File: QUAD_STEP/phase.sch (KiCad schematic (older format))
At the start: 12 parts, among them Q1 BUK9K45-100E,115, Q2 BUK9K45-100E,115

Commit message: beginning layout
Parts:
- Q1, Q2: footprint CUSTOM_FP:TRANS_BUK7K12-60EX -> CUSTOM:TRANS_BUK7K12-60EX; DPN (none) -> 1727-7272-1-ND; MPN (none) -> BUK9K45-100E,115
- R91, R92, R93, R94, R96, R97: footprint (none) -> Resistor_SMD:R_0603_1608Metric_Pad1.05x0.95mm_HandSolder
- R95: footprint (none) -> CUSTOM:WSH2818R0500FEA
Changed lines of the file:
@@
 $Descr A4 11693 8268
 encoding utf-8
-Sheet 3 13
+Sheet 4 13
 Title ""
 Date ""
@@
 AR Path="/5E50B60F/5E4B900F/5E30367B" Ref="Q13"  Part="1"
 AR Path="/5E50B60F/5E4B9032/5E30367B" Ref="Q15"  Part="1"
-F 0 "Q1" H 5400 3000 50  0000 L CNN
+F 0 "Q15" H 5400 3000 50  0000 L CNN
 F 1 "BUK9K45-100E,115" H 5487 2905 50  0001 L CNN
-F 2 "CUSTOM_FP:TRANS_BUK7K12-60EX" H 5400 2875 50  0001 L CIN
+F 2 "CUSTOM:TRANS_BUK7K12-60EX" H 5400 2875 50  0001 L CIN
 F 3 "https://assets.nexperia.com/documents/data-sheet/BUK9K45-100E.pdf" H 5200 2950 50  0001 L CNN
+F 4 "1727-7272-1-ND" H 5200 2950 50  0001 C CNN "DPN"
+F 5 "BUK9K45-100E,115" H 5200 2950 50  0001 C CNN "MPN"
 	1    5200 2950
 	1    0    0    -1
@@
 AR Path="/5E50B60F/5E4B900F/5E303682" Ref="Q14"  Part="1"
 AR Path="/5E50B60F/5E4B9032/5E303682" Ref="Q16"  Part="1"
-F 0 "Q2" H 6300 3000 50  0000 L CNN
+F 0 "Q16" H 6300 3000 50  0000 L CNN
 F 1 "BUK9K45-100E,115" H 6388 2905 50  0001 L CNN
-F 2 "CUSTOM_FP:TRANS_BUK7K12-60EX" H 6300 2875 50  0001 L CIN
+F 2 "CUSTOM:TRANS_BUK7K12-60EX" H 6300 2875 50  0001 L CIN
 F 3 "https://assets.nexperia.com/documents/data-sheet/BUK9K45-100E.pdf" H 6100 2950 50  0001 L CNN
+F 4 "1727-7272-1-ND" H 6100 2950 50  0001 C CNN "DPN"
+F 5 "BUK9K45-100E,115" H 6100 2950 50  0001 C CNN "MPN"
 	1    6100 2950
 	-1   0    0    -1
@@
 AR Path="/5E50B60F/5E4B900F/5E303689" Ref="Q13"  Part="2"
 AR Path="/5E50B60F/5E4B9032/5E303689" Ref="Q15"  Part="2"
-F 0 "Q1" H 5400 4250 50  0000 L CNN
+F 0 "Q15" H 5400 4250 50  0000 L CNN
 F 1 "BUK9K45-100E,115" H 5487 4155 50  0001 L CNN
-F 2 "CUSTOM_FP:TRANS_BUK7K12-60EX" H 5400 4125 50  0001 L CIN
+F 2 "CUSTOM:TRANS_BUK7K12-60EX" H 5400 4125 50  0001 L CIN
 F 3 "https://assets.nexperia.com/documents/data-sheet/BUK9K45-100E.pdf" H 5200 4200 50  0001 L CNN
+F 4 "1727-7272-1-ND" H 5200 4200 50  0001 C CNN "DPN"
+F 5 "BUK9K45-100E,115" H 5200 4200 50  0001 C CNN "MPN"
 	2    5200 4200
 	1    0    0    -1
@@
 AR Path="/5E50B60F/5E4B900F/5E303690" Ref="Q14"  Part="2"
 AR Path="/5E50B60F/5E4B9032/5E303690" Ref="Q16"  Part="2"
-F 0 "Q2" H 6300 4250 50  0000 L CNN
+F 0 "Q16" H 6300 4250 50  0000 L CNN
 F 1 "BUK9K45-100E,115" H 6388 4155 50  0001 L CNN
-F 2 "CUSTOM_FP:TRANS_BUK7K12-60EX" H 6300 4125 50  0001 L CIN
+F 2 "CUSTOM:TRANS_BUK7K12-60EX" H 6300 4125 50  0001 L CIN
 F 3 "https://assets.nexperia.com/documents/data-sheet/BUK9K45-100E.pdf" H 6100 4200 50  0001 L CNN
+F 4 "1727-7272-1-ND" H 6100 4200 50  0001 C CNN "DPN"
+F 5 "BUK9K45-100E,115" H 6100 4200 50  0001 C CNN "MPN"
 	2    6100 4200
 	-1   0    0    -1
@@
 AR Path="/5E50B60F/5E4B900F/5E30369F" Ref="R152"  Part="1"
 AR Path="/5E50B60F/5E4B9032/5E30369F" Ref="R159"  Part="1"
-F 0 "R95" V 5550 4850 50  0000 C CNN
+F 0 "R159" V 5550 4850 50  0000 C CNN
 F 1 "0R022" V 5750 4850 50  0000 C CNN
-F 2 "" V 5580 4850 50  0001 C CNN
+F 2 "CUSTOM:WSH2818R0500FEA" V 5580 4850 50  0001 C CNN
 F 3 "~" H 5650 4850 50  0001 C CNN
 F 4 "WSHM2818R0220FEA" H 5650 4850 50  0001 C CNN "MPN"
@@
 AR Path="/5E50B60F/5E4B900F/5E3036A9" Ref="R149"  Part="1"
 AR Path="/5E50B60F/5E4B9032/5E3036A9" Ref="R156"  Part="1"
-F 0 "R92" V 4700 4200 50  0000 C CNN
+F 0 "R156" V 4700 4200 50  0000 C CNN
 F 1 "22R" V 4900 4200 50  0000 C CNN
-F 2 "" V 4730 4200 50  0001 C CNN
+F 2 "Resistor_SMD:R_0603_1608Metric_Pad1.05x0.95mm_HandSolder" V 4730 4200 50  0001 C CNN
 F 3 "~" H 4800 4200 50  0001 C CNN
 F 4 "ERJ-3EKF22R0V" H 4800 4200 50  0001 C CNN "MPN"
@@
 AR Path="/5E50B60F/5E4B900F/5E3036B3" Ref="R154"  Part="1"
 AR Path="/5E50B60F/5E4B9032/5E3036B3" Ref="R161"  Part="1"
-F 0 "R97" V 6400 4200 50  0000 C CNN
+F 0 "R161" V 6400 4200 50  0000 C CNN
 F 1 "22R" V 6600 4200 50  0000 C CNN
-F 2 "" V 6430 4200 50  0001 C CNN
+F 2 "Resistor_SMD:R_0603_1608Metric_Pad1.05x0.95mm_HandSolder" V 6430 4200 50  0001 C CNN
 F 3 "~" H 6500 4200 50  0001 C CNN
 F 4 "ERJ-3EKF22R0V" H 6500 4200 50  0001 C CNN "MPN"
@@
 AR Path="/5E50B60F/5E4B900F/5E3036BD" Ref="R153"  Part="1"
 AR Path="/5E50B60F/5E4B9032/5E3036BD" Ref="R160"  Part="1"
-F 0 "R96" V 6400 2950 50  0000 C CNN
+F 0 "R160" V 6400 2950 50  0000 C CNN
 F 1 "22R" V 6600 2950 50  0000 C CNN
-F 2 "" V 6430 2950 50  0001 C CNN
+F 2 "Resistor_SMD:R_0603_1608Metric_Pad1.05x0.95mm_HandSolder" V 6430 2950 50  0001 C CNN
 F 3 "~" H 6500 2950 50  0001 C CNN
 F 4 "ERJ-3EKF22R0V" H 6500 2950 50  0001 C CNN "MPN"
@@
 AR Path="/5E50B60F/5E4B900F/5E3036C7" Ref="R148"  Part="1"
 AR Path="/5E50B60F/5E4B9032/5E3036C7" Ref="R155"  Part="1"
-F 0 "R91" V 4700 2950 50  0000 C CNN
+F 0 "R155" V 4700 2950 50  0000 C CNN
 F 1 "22R" V 4900 2950 50  0000 C CNN
-F 2 "" V 4730 2950 50  0001 C CNN
+F 2 "Resistor_SMD:R_0603_1608Metric_Pad1.05x0.95mm_HandSolder" V 4730 2950 50  0001 C CNN
 F 3 "~" H 4800 2950 50  0001 C CNN
 F 4 "ERJ-3EKF22R0V" H 4800 2950 50  0001 C CNN "MPN"
@@
 AR Path="/5E50B60F/5E4B900F/5E3036D1" Ref="R150"  Part="1"
 AR Path="/5E50B60F/5E4B9032/5E3036D1" Ref="R157"  Part="1"
-F 0 "R93" V 5000 4650 50  0000 C CNN
+F 0 "R157" V 5000 4650 50  0000 C CNN
 F 1 "47R" V 5200 4650 50  0000 C CNN
-F 2 "" V 5030 4650 50  0001 C CNN
+F 2 "Resistor_SMD:R_0603_1608Metric_Pad1.05x0.95mm_HandSolder" V 5030 4650 50  0001 C CNN
 F 3 "~" H 5100 4650 50  0001 C CNN
 F 4 "CRGCQ0603F47R" H 5100 4650 50  0001 C CNN "MPN"
@@
 AR Path="/5E50B60F/5E4B900F/5E3036DB" Ref="R151"  Part="1"
 AR Path="/5E50B60F/5E4B9032/5E3036DB" Ref="R158"  Part="1"
-F 0 "R94" V 5000 5050 50  0000 C CNN
+F 0 "R158" V 5000 5050 50  0000 C CNN
 F 1 "47R" V 5200 5050 50  0000 C CNN
-F 2 "" V 5030 5050 50  0001 C CNN
+F 2 "Resistor_SMD:R_0603_1608Metric_Pad1.05x0.95mm_HandSolder" V 5030 5050 50  0001 C CNN
 F 3 "~" H 5100 5050 50  0001 C CNN
 F 4 "CRGCQ0603F47R" H 5100 5050 50  0001 C CNN "MPN"
@@
 AR Path="/5E50B60F/5E4B900F/5E3036E5" Ref="C80"  Part="1"
 AR Path="/5E50B60F/5E4B9032/5E3036E5" Ref="C83"  Part="1"
-F 0 "C29" H 6265 2346 50  0000 L CNN
+F 0 "C83" H 6265 2346 50  0000 L CNN
 F 1 "470n" H 6265 2255 50  0000 L CNN
 F 2 "Capacitor_SMD:C_0603_1608Metric" H 6188 2150 50  0001 C CNN
@@
 AR Path="/5E50B60F/5E4B900F/5E3036EF" Ref="C78"  Part="1"
 AR Path="/5E50B60F/5E4B9032/5E3036EF" Ref="C81"  Part="1"
-F 0 "C27" V 5000 3450 50  0000 L BNN
+F 0 "C81" V 5000 3450 50  0000 L BNN
 F 1 "220n" V 5000 3350 50  0000 R BNN
 F 2 "Capacitor_SMD:C_0603_1608Metric" H 5038 3250 50  0001 C CNN
@@
 AR Path="/5E50B60F/5E4B900F/5E303702" Ref="C79"  Part="1"
 AR Path="/5E50B60F/5E4B9032/5E303702" Ref="C82"  Part="1"
-F 0 "C28" V 5000 3650 50  0000 L BNN
+F 0 "C82" V 5000 3650 50  0000 L BNN
 F 1 "220n" V 5000 3550 50  0000 R BNN
 F 2 "Capacitor_SMD:C_0603_1608Metric" H 5038 3450 50  0001 C CNN

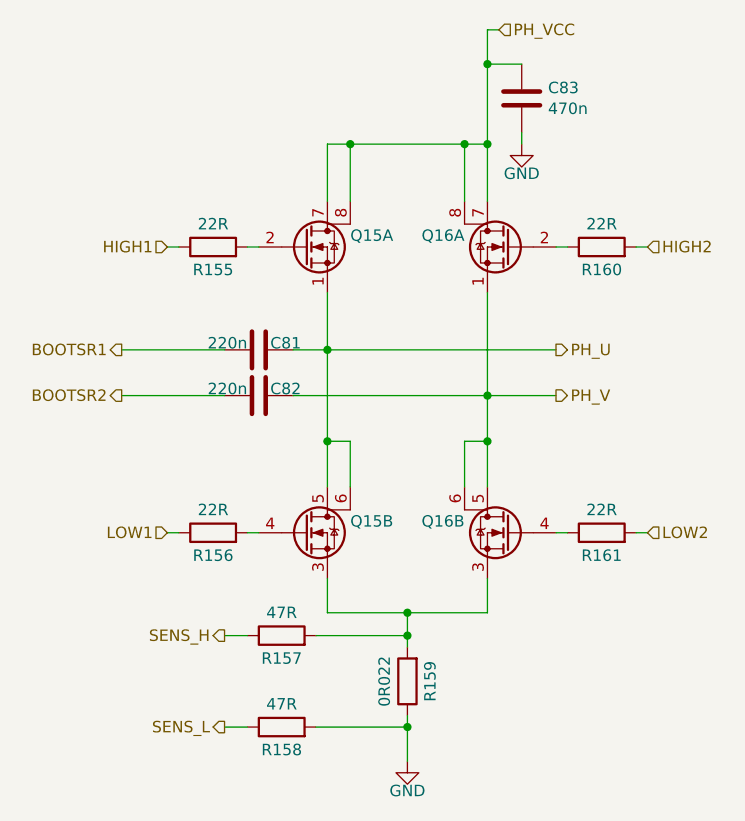
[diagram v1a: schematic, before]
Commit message: changed scope to 5 axis, preliminary completion of component positioning
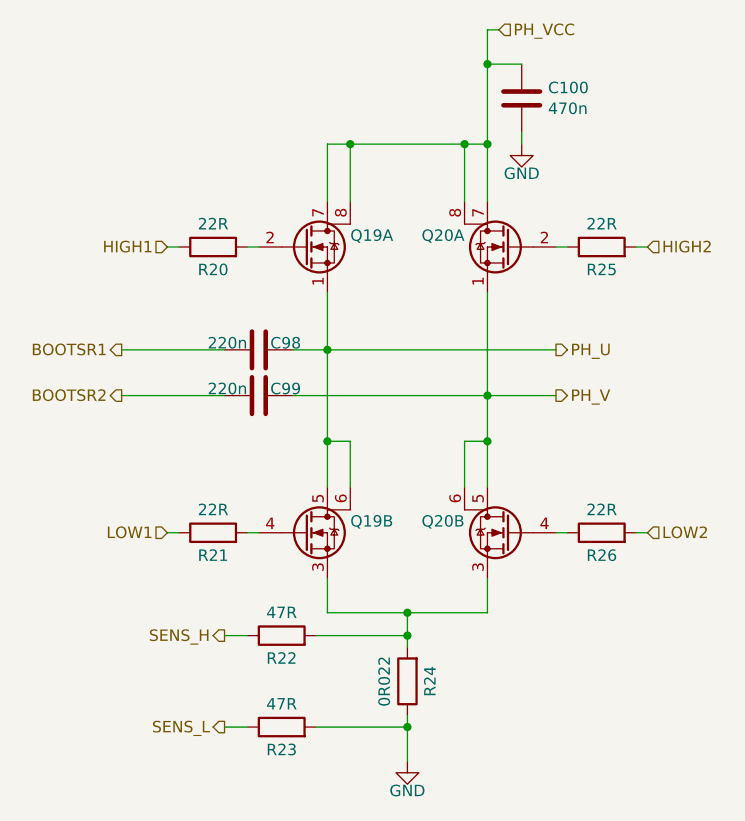
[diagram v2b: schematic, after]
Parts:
- Q1, Q2: footprint CUSTOM:TRANS_BUK7K12-60EX -> CUSTOM_FP:TRANS_BUK7K12-60EX
- R95: footprint CUSTOM:WSH2818R0500FEA -> CUSTOM_FP:WSH2818R0500FEA
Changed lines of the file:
@@
 EESchema Schematic File Version 4
-EELAYER 30 0
+LIBS:QUAD_STEP-cache
+EELAYER 26 0
 EELAYER END
 $Descr A4 11693 8268
 encoding utf-8
-Sheet 4 13
+Sheet 15 16
 Title ""
 Date ""
@@
 AR Path="/5E50B60F/5E4B900F/5E30367B" Ref="Q13"  Part="1"
 AR Path="/5E50B60F/5E4B9032/5E30367B" Ref="Q15"  Part="1"
-F 0 "Q15" H 5400 3000 50  0000 L CNN
+AR Path="/5F24B60D/5E4B900F/5E30367B" Ref="Q17"  Part="1"
+AR Path="/5F24B60D/5E4B9032/5E30367B" Ref="Q19"  Part="1"
+F 0 "Q19" H 5400 3000 50  0000 L CNN
 F 1 "BUK9K45-100E,115" H 5487 2905 50  0001 L CNN
-F 2 "CUSTOM:TRANS_BUK7K12-60EX" H 5400 2875 50  0001 L CIN
+F 2 "CUSTOM_FP:TRANS_BUK7K12-60EX" H 5400 2875 50  0001 L CIN
 F 3 "https://assets.nexperia.com/documents/data-sheet/BUK9K45-100E.pdf" H 5200 2950 50  0001 L CNN
 F 4 "1727-7272-1-ND" H 5200 2950 50  0001 C CNN "DPN"
@@
 AR Path="/5E50B60F/5E4B900F/5E303682" Ref="Q14"  Part="1"
 AR Path="/5E50B60F/5E4B9032/5E303682" Ref="Q16"  Part="1"
-F 0 "Q16" H 6300 3000 50  0000 L CNN
+AR Path="/5F24B60D/5E4B900F/5E303682" Ref="Q18"  Part="1"
+AR Path="/5F24B60D/5E4B9032/5E303682" Ref="Q20"  Part="1"
+F 0 "Q20" H 6300 3000 50  0000 L CNN
 F 1 "BUK9K45-100E,115" H 6388 2905 50  0001 L CNN
-F 2 "CUSTOM:TRANS_BUK7K12-60EX" H 6300 2875 50  0001 L CIN
+F 2 "CUSTOM_FP:TRANS_BUK7K12-60EX" H 6300 2875 50  0001 L CIN
 F 3 "https://assets.nexperia.com/documents/data-sheet/BUK9K45-100E.pdf" H 6100 2950 50  0001 L CNN
 F 4 "1727-7272-1-ND" H 6100 2950 50  0001 C CNN "DPN"
@@
 AR Path="/5E50B60F/5E4B900F/5E303689" Ref="Q13"  Part="2"
 AR Path="/5E50B60F/5E4B9032/5E303689" Ref="Q15"  Part="2"
-F 0 "Q15" H 5400 4250 50  0000 L CNN
+AR Path="/5F24B60D/5E4B900F/5E303689" Ref="Q17"  Part="2"
+AR Path="/5F24B60D/5E4B9032/5E303689" Ref="Q19"  Part="2"
+F 0 "Q19" H 5400 4250 50  0000 L CNN
 F 1 "BUK9K45-100E,115" H 5487 4155 50  0001 L CNN
-F 2 "CUSTOM:TRANS_BUK7K12-60EX" H 5400 4125 50  0001 L CIN
+F 2 "CUSTOM_FP:TRANS_BUK7K12-60EX" H 5400 4125 50  0001 L CIN
 F 3 "https://assets.nexperia.com/documents/data-sheet/BUK9K45-100E.pdf" H 5200 4200 50  0001 L CNN
 F 4 "1727-7272-1-ND" H 5200 4200 50  0001 C CNN "DPN"
@@
 AR Path="/5E50B60F/5E4B900F/5E303690" Ref="Q14"  Part="2"
 AR Path="/5E50B60F/5E4B9032/5E303690" Ref="Q16"  Part="2"
-F 0 "Q16" H 6300 4250 50  0000 L CNN
+AR Path="/5F24B60D/5E4B900F/5E303690" Ref="Q18"  Part="2"
+AR Path="/5F24B60D/5E4B9032/5E303690" Ref="Q20"  Part="2"
+F 0 "Q20" H 6300 4250 50  0000 L CNN
 F 1 "BUK9K45-100E,115" H 6388 4155 50  0001 L CNN
 F 2 "CUSTOM:TRANS_BUK7K12-60EX" H 6300 4125 50  0001 L CIN
@@
 AR Path="/5E50B60F/5E4B900F/5E303697" Ref="#PWR091"  Part="1"
 AR Path="/5E50B60F/5E4B9032/5E303697" Ref="#PWR093"  Part="1"
-F 0 "#PWR093" H 5650 4950 50  0001 C CNN
+AR Path="/5F24B60D/5E4B900F/5E303697" Ref="#PWR0109"  Part="1"
+AR Path="/5F24B60D/5E4B9032/5E303697" Ref="#PWR0111"  Part="1"
+F 0 "#PWR0111" H 5650 4950 50  0001 C CNN
 F 1 "GND" H 5650 5100 50  0000 C TNN
 F 2 "" H 5650 5200 50  0001 C CNN
@@
 AR Path="/5E50B60F/5E4B900F/5E30369F" Ref="R152"  Part="1"
 AR Path="/5E50B60F/5E4B9032/5E30369F" Ref="R159"  Part="1"
-F 0 "R159" V 5550 4850 50  0000 C CNN
+AR Path="/5F24B60D/5E4B900F/5E30369F" Ref="R17"  Part="1"
+AR Path="/5F24B60D/5E4B9032/5E30369F" Ref="R24"  Part="1"
+F 0 "R24" V 5550 4850 50  0000 C CNN
 F 1 "0R022" V 5750 4850 50  0000 C CNN
-F 2 "CUSTOM:WSH2818R0500FEA" V 5580 4850 50  0001 C CNN
+F 2 "CUSTOM_FP:WSH2818R0500FEA" V 5580 4850 50  0001 C CNN
 F 3 "~" H 5650 4850 50  0001 C CNN
 F 4 "WSHM2818R0220FEA" H 5650 4850 50  0001 C CNN "MPN"
@@
 AR Path="/5E50B60F/5E4B900F/5E3036A9" Ref="R149"  Part="1"
 AR Path="/5E50B60F/5E4B9032/5E3036A9" Ref="R156"  Part="1"
-F 0 "R156" V 4700 4200 50  0000 C CNN
+AR Path="/5F24B60D/5E4B900F/5E3036A9" Ref="R14"  Part="1"
+AR Path="/5F24B60D/5E4B9032/5E3036A9" Ref="R21"  Part="1"
+F 0 "R21" V 4700 4200 50  0000 C CNN
 F 1 "22R" V 4900 4200 50  0000 C CNN
 F 2 "Resistor_SMD:R_0603_1608Metric_Pad1.05x0.95mm_HandSolder" V 4730 4200 50  0001 C CNN
@@
 AR Path="/5E50B60F/5E4B900F/5E3036B3" Ref="R154"  Part="1"
 AR Path="/5E50B60F/5E4B9032/5E3036B3" Ref="R161"  Part="1"
-F 0 "R161" V 6400 4200 50  0000 C CNN
+AR Path="/5F24B60D/5E4B900F/5E3036B3" Ref="R19"  Part="1"
+AR Path="/5F24B60D/5E4B9032/5E3036B3" Ref="R26"  Part="1"
+F 0 "R26" V 6400 4200 50  0000 C CNN
 F 1 "22R" V 6600 4200 50  0000 C CNN
 F 2 "Resistor_SMD:R_0603_1608Metric_Pad1.05x0.95mm_HandSolder" V 6430 4200 50  0001 C CNN
@@
 AR Path="/5E50B60F/5E4B900F/5E3036BD" Ref="R153"  Part="1"
 AR Path="/5E50B60F/5E4B9032/5E3036BD" Ref="R160"  Part="1"
-F 0 "R160" V 6400 2950 50  0000 C CNN
+AR Path="/5F24B60D/5E4B900F/5E3036BD" Ref="R18"  Part="1"
+AR Path="/5F24B60D/5E4B9032/5E3036BD" Ref="R25"  Part="1"
+F 0 "R25" V 6400 2950 50  0000 C CNN
 F 1 "22R" V 6600 2950 50  0000 C CNN
 F 2 "Resistor_SMD:R_0603_1608Metric_Pad1.05x0.95mm_HandSolder" V 6430 2950 50  0001 C CNN
@@
 AR Path="/5E50B60F/5E4B900F/5E3036C7" Ref="R148"  Part="1"
 AR Path="/5E50B60F/5E4B9032/5E3036C7" Ref="R155"  Part="1"
-F 0 "R155" V 4700 2950 50  0000 C CNN
+AR Path="/5F24B60D/5E4B900F/5E3036C7" Ref="R13"  Part="1"
+AR Path="/5F24B60D/5E4B9032/5E3036C7" Ref="R20"  Part="1"
+F 0 "R20" V 4700 2950 50  0000 C CNN
 F 1 "22R" V 4900 2950 50  0000 C CNN
 F 2 "Resistor_SMD:R_0603_1608Metric_Pad1.05x0.95mm_HandSolder" V 4730 2950 50  0001 C CNN
@@
 AR Path="/5E50B60F/5E4B900F/5E3036D1" Ref="R150"  Part="1"
 AR Path="/5E50B60F/5E4B9032/5E3036D1" Ref="R157"  Part="1"
-F 0 "R157" V 5000 4650 50  0000 C CNN
+AR Path="/5F24B60D/5E4B900F/5E3036D1" Ref="R15"  Part="1"
+AR Path="/5F24B60D/5E4B9032/5E3036D1" Ref="R22"  Part="1"
+F 0 "R22" V 5000 4650 50  0000 C CNN
 F 1 "47R" V 5200 4650 50  0000 C CNN
 F 2 "Resistor_SMD:R_0603_1608Metric_Pad1.05x0.95mm_HandSolder" V 5030 4650 50  0001 C CNN
@@
 AR Path="/5E50B60F/5E4B900F/5E3036DB" Ref="R151"  Part="1"
 AR Path="/5E50B60F/5E4B9032/5E3036DB" Ref="R158"  Part="1"
-F 0 "R158" V 5000 5050 50  0000 C CNN
+AR Path="/5F24B60D/5E4B900F/5E3036DB" Ref="R16"  Part="1"
+AR Path="/5F24B60D/5E4B9032/5E3036DB" Ref="R23"  Part="1"
+F 0 "R23" V 5000 5050 50  0000 C CNN
 F 1 "47R" V 5200 5050 50  0000 C CNN
 F 2 "Resistor_SMD:R_0603_1608Metric_Pad1.05x0.95mm_HandSolder" V 5030 5050 50  0001 C CNN
@@
 AR Path="/5E50B60F/5E4B900F/5E3036E5" Ref="C80"  Part="1"
 AR Path="/5E50B60F/5E4B9032/5E3036E5" Ref="C83"  Part="1"
-F 0 "C83" H 6265 2346 50  0000 L CNN
+AR Path="/5F24B60D/5E4B900F/5E3036E5" Ref="C97"  Part="1"
+AR Path="/5F24B60D/5E4B9032/5E3036E5" Ref="C100"  Part="1"
+F 0 "C100" H 6265 2346 50  0000 L CNN
 F 1 "470n" H 6265 2255 50  0000 L CNN
 F 2 "Capacitor_SMD:C_0603_1608Metric" H 6188 2150 50  0001 C CNN
@@
 AR Path="/5E50B60F/5E4B900F/5E3036EF" Ref="C78"  Part="1"
 AR Path="/5E50B60F/5E4B9032/5E3036EF" Ref="C81"  Part="1"
-F 0 "C81" V 5000 3450 50  0000 L BNN
+AR Path="/5F24B60D/5E4B900F/5E3036EF" Ref="C95"  Part="1"
+AR Path="/5F24B60D/5E4B9032/5E3036EF" Ref="C98"  Part="1"
+F 0 "C98" V 5000 3450 50  0000 L BNN
 F 1 "220n" V 5000 3350 50  0000 R BNN
 F 2 "Capacitor_SMD:C_0603_1608Metric" H 5038 3250 50  0001 C CNN
@@
 AR Path="/5E50B60F/5E4B900F/5E303702" Ref="C79"  Part="1"
 AR Path="/5E50B60F/5E4B9032/5E303702" Ref="C82"  Part="1"
-F 0 "C82" V 5000 3650 50  0000 L BNN
+AR Path="/5F24B60D/5E4B900F/5E303702" Ref="C96"  Part="1"
+AR Path="/5F24B60D/5E4B9032/5E303702" Ref="C99"  Part="1"
+F 0 "C99" V 5000 3650 50  0000 L BNN
 F 1 "220n" V 5000 3550 50  0000 R BNN
 F 2 "Capacitor_SMD:C_0603_1608Metric" H 5038 3450 50  0001 C CNN
@@
 AR Path="/5E50B60F/5E4B900F/5E303736" Ref="#PWR092"  Part="1"
 AR Path="/5E50B60F/5E4B9032/5E303736" Ref="#PWR094"  Part="1"
-F 0 "#PWR094" H 6150 2250 50  0001 C CNN
+AR Path="/5F24B60D/5E4B900F/5E303736" Ref="#PWR0110"  Part="1"
+AR Path="/5F24B60D/5E4B9032/5E303736" Ref="#PWR0112"  Part="1"
+F 0 "#PWR0112" H 6150 2250 50  0001 C CNN
 F 1 "GND" H 6150 2400 50  0000 C TNN
 F 2 "" H 6150 2500 50  0001 C CNN
